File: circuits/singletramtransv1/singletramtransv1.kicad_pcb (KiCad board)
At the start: 2 copper layers, 56.6 x 57.7 mm, 25 parts, among them J1 Power 9V, J2 Signal in, Q1 S9013

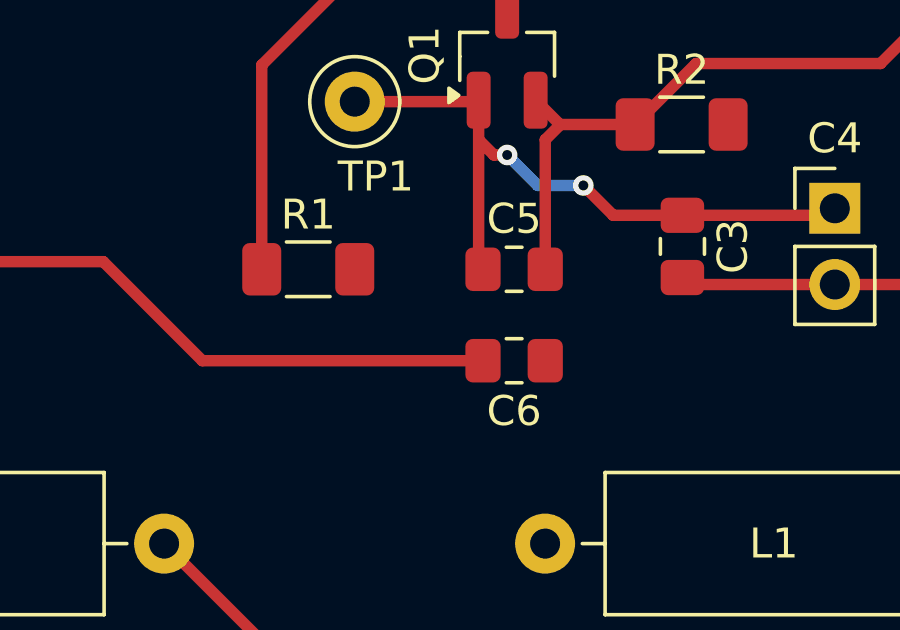
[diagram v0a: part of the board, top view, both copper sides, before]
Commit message: Updating the single transistor AM test transmitter project
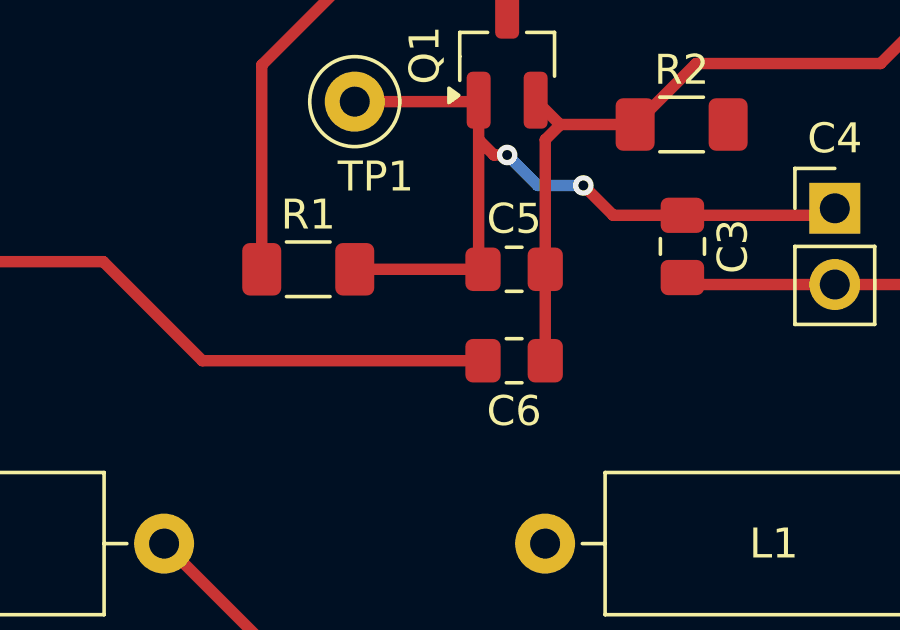
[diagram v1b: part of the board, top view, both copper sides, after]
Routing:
- net Net-(Q1-B): track 22.9 -> 27.1 mm
- net Net-(Q1-E): track 22.9 -> 26.0 mm
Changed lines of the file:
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@@
 		(grid_origin 100 100)
 		(pcbplotparams
-			(layerselection 0x00010a8_80000001)
+			(layerselection 0x00010e8_ffffffff)
 			(plot_on_all_layers_selection 0x0000000_00000000)
 			(disableapertmacros no)
@@
 			(drillshape 0)
 			(scaleselection 1)
-			(outputdirectory "")
+			(outputdirectory "gerber")
 		)
 	)
@@
 		(tags "CP Radial series Radial pin pitch 2.50mm  diameter 6.3mm Electrolytic Capacitor")
 		(property "Reference" "C1"
-			(at 1.25 -4.4 270)
+			(at 1.25 -4.4 -90)
 			(layer "F.SilkS")
 			(effects
@@
 		)
 		(property "Value" "100uF"
-			(at 1.25 4.4 270)
+			(at 1.25 4.4 -90)
 			(layer "F.Fab")
 			(effects
@@
 		)
 		(fp_text user "${REFERENCE}"
-			(at 1.25 0 270)
+			(at 1.25 0 -90)
 			(layer "F.Fab")
 			(effects
@@
 		(tags "SOT-23")
 		(property "Reference" "Q1"
-			(at 0 -2.75 270)
+			(at 0 -2.75 -90)
 			(layer "F.SilkS")
 			(effects
@@
 		)
 		(property "Value" "S9013"
-			(at 0 2.5 270)
+			(at 0 2.5 -90)
 			(layer "F.Fab")
 			(effects
@@
 		)
 		(fp_text user "${REFERENCE}"
-			(at 0 0 360)
+			(at 0 0 0)
 			(layer "F.Fab")
 			(effects
@@
 		(tags "resistor handsolder")
 		(property "Reference" "R2"
-			(at 0 -1.82 360)
+			(at 0 -1.82 0)
 			(layer "F.SilkS")
 			(effects
@@
 		)
 		(property "Value" "R"
-			(at 0 1.82 360)
+			(at 0 1.82 0)
 			(layer "F.Fab")
 			(effects
@@
 		)
 		(fp_text user "${REFERENCE}"
-			(at 0 0 360)
+			(at 0 0 0)
 			(layer "F.Fab")
 			(effects
@@
 		(layer "Edge.Cuts")
 	)
+	(dimension
+		(type aligned)
+		(layer "Edge.Cuts")
+		(pts
+			(xy 156.642 42.342) (xy 156.642 100)
+		)
+		(height -11.938)
+		(gr_text "57.6580 mm"
+			(at 167.43 71.171 90)
+			(layer "Edge.Cuts")
+			(effects
+				(font
+					(size 1 1)
+					(thickness 0.15)
+				)
+			)
+		)
+		(format
+			(prefix "")
+			(suffix "")
+			(units 3)
+			(units_format 1)
+			(precision 4)
+		)
+		(style
+			(thickness 0.1)
+			(arrow_length 1.27)
+			(text_position_mode 0)
+			(extension_height 0.58642)
+			(extension_offset 0.5) keep_text_aligned)
+	)
+	(dimension
+		(type aligned)
+		(layer "Edge.Cuts")
+		(pts
+			(xy 100 42.342) (xy 156.642 42.342)
+		)
+		(height 73.152)
+		(gr_text "56.6420 mm"
+			(at 128.321 114.344 0)
+			(layer "Edge.Cuts")
+			(effects
+				(font
+					(size 1 1)
+					(thickness 0.15)
+				)
+			)
+		)
+		(format
+			(prefix "")
+			(suffix "")
+			(units 3)
+			(units_format 1)
+			(precision 4)
+		)
+		(style
+			(thickness 0.1)
+			(arrow_length 1.27)
+			(text_position_mode 0)
+			(extension_height 0.58642)
+			(extension_offset 0.5) keep_text_aligned)
+	)
 	(segment
 		(start 122.347 77.394)
@@
 	)
 	(segment
+		(start 128.702 68.25)
+		(end 132.977 68.25)
+		(width 0.381)
+		(layer "F.Cu")
+		(net 7)
+	)
+	(segment
 		(start 133.34 64.44)
 		(end 132.832 63.932)
@@
 		(width 0.381)
 		(layer "F.Cu")
+		(net 8)
+	)
+	(segment
+		(start 135.052 71.298)
+		(end 135.052 68.25)
+		(width 0.381)
+		(layer "F.Cu")
